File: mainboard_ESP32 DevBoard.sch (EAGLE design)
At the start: 38 parts, among them IC1 LM358N, IC2 LM833N, IC3 74HC08N, K1 AQH213, X1 JST-XH-02-PIN-LONG-PAD, X2 JST-XH-04-PIN-LONG-PAD, X3 1751248, X4 1751248

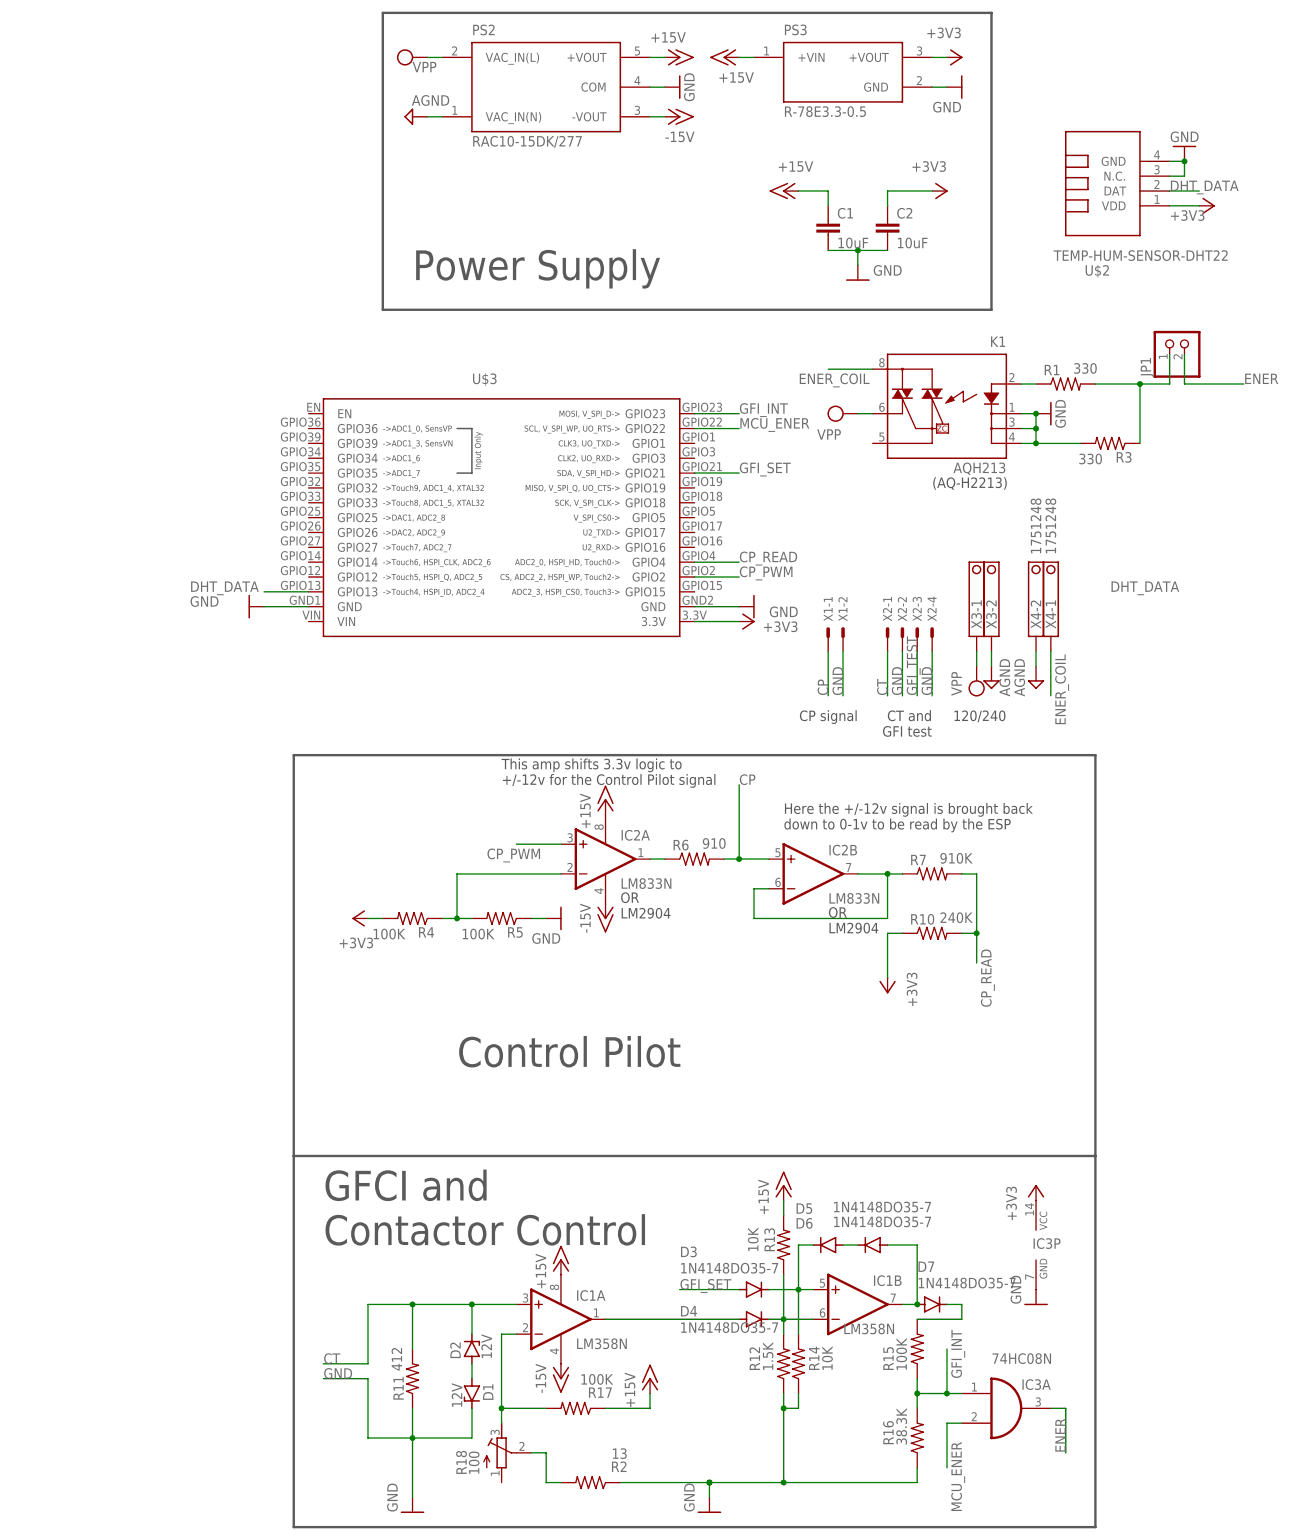
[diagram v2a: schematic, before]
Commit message: Added header to disconnect 3.3v output from esp to 3.3 rail. Added LED to indicate when contactor is energized. Added I2C connector. Added mounting holes.
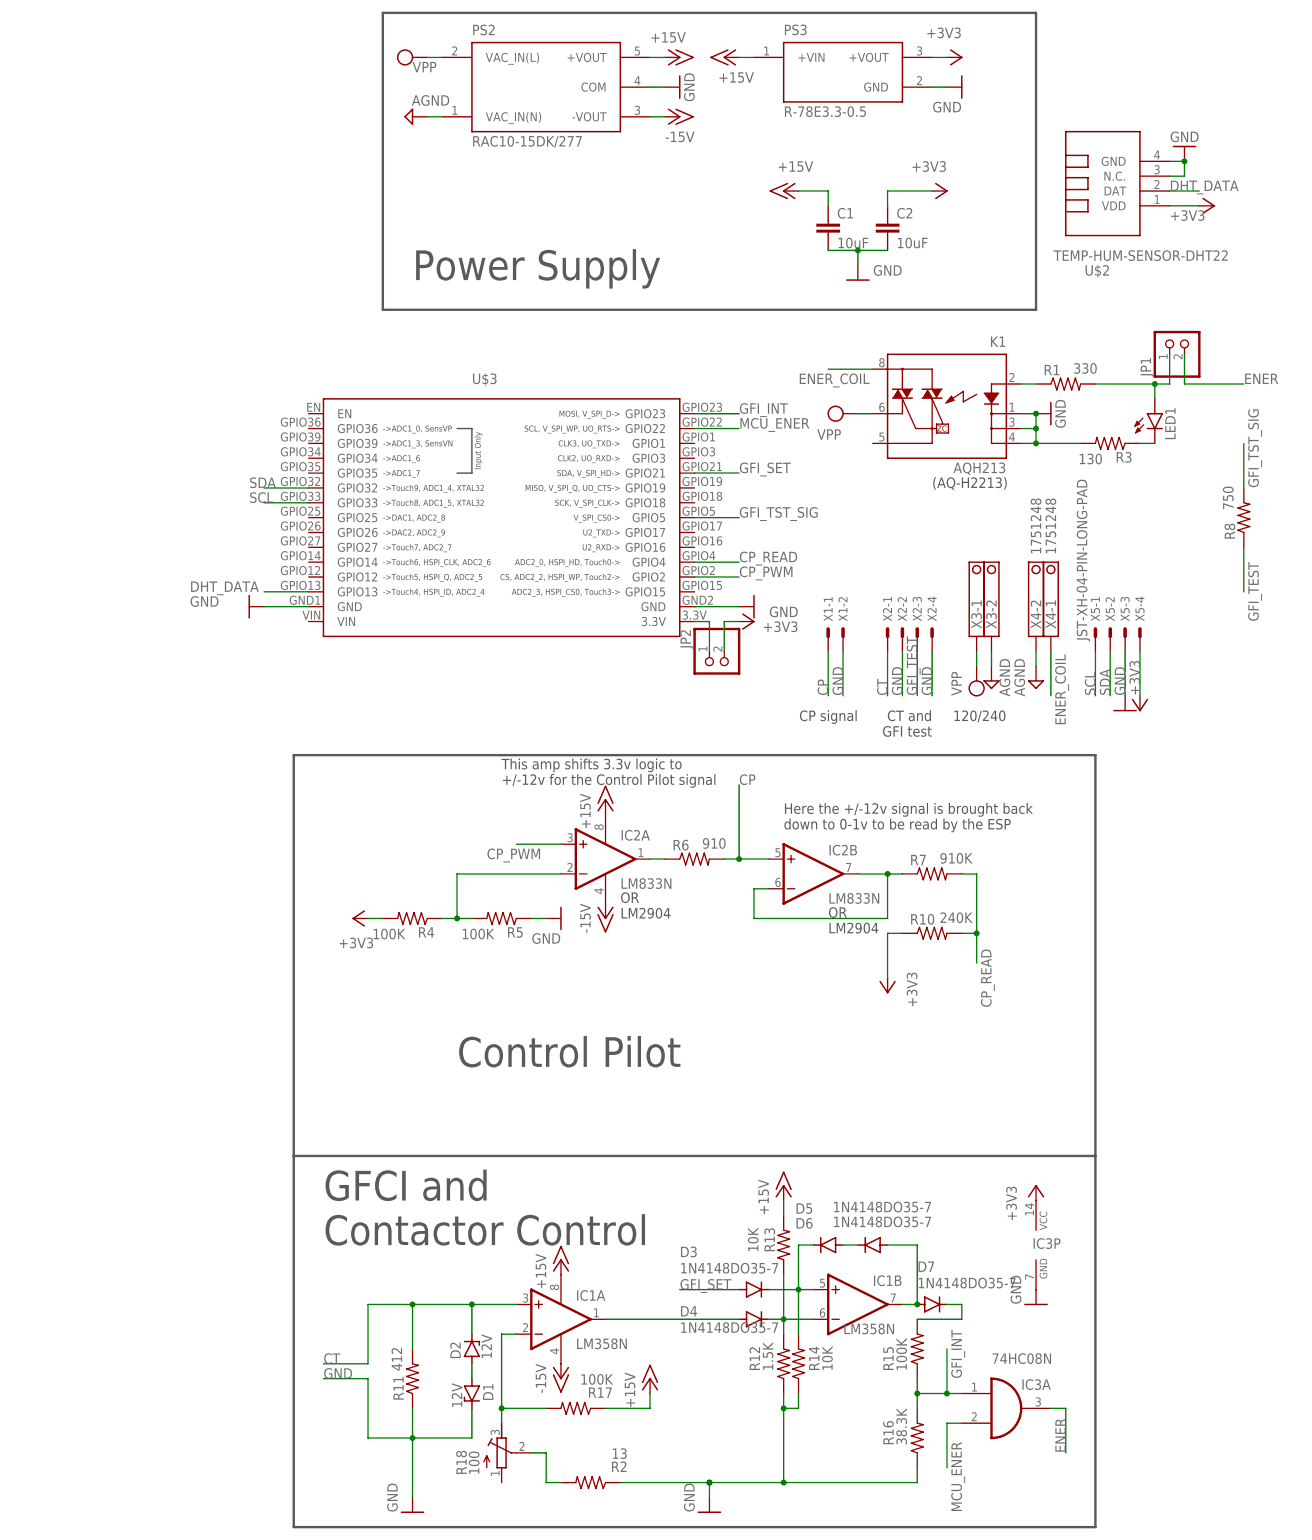
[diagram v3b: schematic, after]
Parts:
- added JP2: (no value), pinhead:PINHD-1X2/90
- added LED1: (no value), led:LED3MM
- added R8: 750, rcl:R-US_0204/7
- added X5: JST-XH-04-PIN-LONG-PAD, Rembrandt Electronics - JST XH Connectors v1-0:JST-XH-04-PIN-LONG-PAD
- R3: value 330 -> 130
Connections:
- new net GFI_TST_SIG: R8.2, U$3.GPIO5
- new net N$10: JP2.1, U$3.3.3V
- new net N$8: LED1.C, R3.1
- new net SCL: U$3.GPIO33, X5-1.S
- new net SDA: U$3.GPIO32, X5-2.S
- net +3V3: now also JP2.2, X5-4.S; no longer U$3.3.3V
- net GFI_TEST: now also R8.1
- net GND: now also X5-3.S
- net N$3: now also LED1.A; no longer R3.1
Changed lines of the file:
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@@
 <part name="GND4" library="supply1" library_urn="urn:adsk.eagle:library:371" deviceset="GND" device=""/>
 <part name="JP1" library="pinhead" library_urn="urn:adsk.eagle:library:325" deviceset="PINHD-1X2" device="" package3d_urn="urn:adsk.eagle:package:22435/2"/>
-<part name="R3" library="rcl" library_urn="urn:adsk.eagle:library:334" deviceset="R-US_" device="0204/7" package3d_urn="urn:adsk.eagle:package:23498/2" value="330"/>
+<part name="R3" library="rcl" library_urn="urn:adsk.eagle:library:334" deviceset="R-US_" device="0204/7" package3d_urn="urn:adsk.eagle:package:23498/2" value="130"/>
 <part name="P+5" library="supply1" library_urn="urn:adsk.eagle:library:371" deviceset="+15V" device=""/>
 <part name="P+6" library="supply1" library_urn="urn:adsk.eagle:library:371" deviceset="+15V" device=""/>
@@
 <part name="P+7" library="supply1" library_urn="urn:adsk.eagle:library:371" deviceset="+15V" device=""/>
 <part name="D7" library="diode" library_urn="urn:adsk.eagle:library:210" deviceset="1N4148" device="DO35-7" package3d_urn="urn:adsk.eagle:package:43339/2"/>
+<part name="LED1" library="led" library_urn="urn:adsk.eagle:library:259" deviceset="LED" device="3MM" package3d_urn="urn:adsk.eagle:package:15797/1"/>
+<part name="JP2" library="pinhead" library_urn="urn:adsk.eagle:library:325" deviceset="PINHD-1X2" device="/90" package3d_urn="urn:adsk.eagle:package:22437/2"/>
+<part name="R8" library="rcl" library_urn="urn:adsk.eagle:library:334" deviceset="R-US_" device="0204/7" package3d_urn="urn:adsk.eagle:package:23498/2" value="750"/>
+<part name="X5" library="Rembrandt Electronics - JST XH Connectors v1-0" deviceset="JST-XH-04-PIN" device="-LONG-PAD"/>
+<part name="GND7" library="supply1" library_urn="urn:adsk.eagle:library:371" deviceset="GND" device=""/>
+<part name="+3V1" library="supply1" library_urn="urn:adsk.eagle:library:371" deviceset="+3V3" device=""/>
 </parts>
 <sheets>
@@
 <text x="114.3" y="33.02" size="1.778" layer="97" rot="R180">120/240</text>
 <wire x1="7.62" y1="152.4" x2="7.62" y2="101.6" width="0.4064" layer="97"/>
-<wire x1="7.62" y1="101.6" x2="111.76" y2="101.6" width="0.4064" layer="97"/>
-<wire x1="111.76" y1="101.6" x2="111.76" y2="152.4" width="0.4064" layer="97"/>
-<wire x1="111.76" y1="152.4" x2="7.62" y2="152.4" width="0.4064" layer="97"/>
+<wire x1="7.62" y1="101.6" x2="119.38" y2="101.6" width="0.4064" layer="97"/>
+<wire x1="119.38" y1="101.6" x2="119.38" y2="152.4" width="0.4064" layer="97"/>
+<wire x1="119.38" y1="152.4" x2="7.62" y2="152.4" width="0.4064" layer="97"/>
 <text x="12.7" y="106.68" size="5.08" layer="97">Power Supply</text>
 </plain>
@@
 <attribute name="NAME" x="99.06" y="-63.0174" size="1.778" layer="95"/>
 <attribute name="VALUE" x="99.06" y="-65.8114" size="1.778" layer="96"/>
+</instance>
+<instance part="LED1" gate="G$1" x="139.7" y="83.82" smashed="yes">
+<attribute name="NAME" x="143.256" y="79.248" size="1.778" layer="95" rot="R90"/>
+<attribute name="VALUE" x="145.415" y="79.248" size="1.778" layer="96" rot="R90"/>
+</instance>
+<instance part="JP2" gate="G$1" x="66.04" y="40.64" smashed="yes" rot="MR270">
+<attribute name="NAME" x="60.325" y="46.99" size="1.778" layer="95" rot="MR270"/>
+<attribute name="VALUE" x="71.12" y="46.99" size="1.778" layer="96" rot="MR270"/>
+</instance>
+<instance part="R8" gate="G$1" x="154.94" y="66.04" smashed="yes" rot="R90">
+<attribute name="NAME" x="153.4414" y="62.23" size="1.778" layer="95" rot="R90"/>
+<attribute name="VALUE" x="153.162" y="67.31" size="1.778" layer="96" rot="R90"/>
+</instance>
+<instance part="X5" gate="-1" x="129.54" y="45.72" smashed="yes" rot="R90">
+<attribute name="NAME" x="130.302" y="48.26" size="1.524" layer="95" rot="R90"/>
+<attribute name="VALUE" x="128.143" y="44.958" size="1.778" layer="96" rot="R90"/>
+</instance>
+<instance part="X5" gate="-2" x="132.08" y="45.72" smashed="yes" rot="R90">
+<attribute name="NAME" x="132.842" y="48.26" size="1.524" layer="95" rot="R90"/>
+</instance>
+<instance part="X5" gate="-3" x="134.62" y="45.72" smashed="yes" rot="R90">
+<attribute name="NAME" x="135.382" y="48.26" size="1.524" layer="95" rot="R90"/>
+</instance>
+<instance part="X5" gate="-4" x="137.16" y="45.72" smashed="yes" rot="R90">
+<attribute name="NAME" x="137.922" y="48.26" size="1.524" layer="95" rot="R90"/>
+</instance>
+<instance part="GND7" gate="1" x="134.62" y="33.02" smashed="yes">
+<attribute name="VALUE" x="134.62" y="35.56" size="1.778" layer="96" rot="R90"/>
+</instance>
+<instance part="+3V1" gate="G$1" x="137.16" y="33.02" smashed="yes" rot="R180">
+<attribute name="VALUE" x="137.16" y="35.56" size="1.778" layer="96" rot="R90"/>
 </instance>
 </instances>
@@
 <wire x1="60.96" y1="50.8" x2="68.58" y2="50.8" width="0.1524" layer="91"/>
 </segment>
+<segment>
+<pinref part="X5" gate="-3" pin="S"/>
+<wire x1="134.62" y1="43.18" x2="134.62" y2="35.56" width="0.1524" layer="91"/>
+<pinref part="GND7" gate="1" pin="GND"/>
+</segment>
 </net>
 <net name="+3V3" class="0">
@@
 <pinref part="+3V2" gate="G$1" pin="+3V3"/>
 <wire x1="142.24" y1="119.38" x2="147.32" y2="119.38" width="0.1524" layer="91"/>
-</segment>
-<segment>
-<pinref part="+3V5" gate="G$1" pin="+3V3"/>
-<pinref part="PS3" gate="G$1" pin="+VOUT"/>
-<wire x1="104.14" y1="144.78" x2="101.6" y2="144.78" width="0.1524" layer="91"/>
 </segment>
 <segment>
@@
 <segment>
 <pinref part="+3V8" gate="G$1" pin="+3V3"/>
-<pinref part="U$3" gate="G$1" pin="3.3V"/>
-<wire x1="68.58" y1="48.26" x2="60.96" y2="48.26" width="0.1524" layer="91"/>
+<wire x1="68.58" y1="48.26" x2="66.04" y2="48.26" width="0.1524" layer="91"/>
+<pinref part="JP2" gate="G$1" pin="2"/>
+<wire x1="66.04" y1="43.18" x2="66.04" y2="48.26" width="0.1524" layer="91"/>
+</segment>
+<segment>
+<pinref part="PS3" gate="G$1" pin="+VOUT"/>
+<pinref part="+3V5" gate="G$1" pin="+3V3"/>
+<wire x1="101.6" y1="144.78" x2="104.14" y2="144.78" width="0.1524" layer="91"/>
+</segment>
+<segment>
+<pinref part="X5" gate="-4" pin="S"/>
+<wire x1="137.16" y1="43.18" x2="137.16" y2="35.56" width="0.1524" layer="91"/>
+<pinref part="+3V1" gate="G$1" pin="+3V3"/>
 </segment>
 </net>
@@
 <label x="99.06" y="35.56" size="1.778" layer="95" rot="R90"/>
 </segment>
+<segment>
+<wire x1="154.94" y1="60.96" x2="154.94" y2="53.34" width="0.1524" layer="91"/>
+<pinref part="R8" gate="G$1" pin="1"/>
+<label x="157.48" y="48.26" size="1.778" layer="95" rot="R90"/>
+</segment>
 </net>
 <net name="N$6" class="0">
@@
 <pinref part="U$3" gate="G$1" pin="GPIO13"/>
 <wire x1="-5.08" y1="53.34" x2="-12.7" y2="53.34" width="0.1524" layer="91"/>
-<label x="132.08" y="53.34" size="1.778" layer="95"/>
 <label x="-25.4" y="53.34" size="1.778" layer="95"/>
 </segment>
@@
 <pinref part="R1" gate="G$1" pin="2"/>
 <wire x1="142.24" y1="93.98" x2="142.24" y2="88.9" width="0.1524" layer="91"/>
-<wire x1="142.24" y1="88.9" x2="137.16" y2="88.9" width="0.1524" layer="91"/>
-<pinref part="R3" gate="G$1" pin="1"/>
-<wire x1="137.16" y1="88.9" x2="129.54" y2="88.9" width="0.1524" layer="91"/>
-<wire x1="137.16" y1="78.74" x2="137.16" y2="88.9" width="0.1524" layer="91"/>
-<junction x="137.16" y="88.9"/>
+<wire x1="142.24" y1="88.9" x2="139.7" y2="88.9" width="0.1524" layer="91"/>
+<pinref part="LED1" gate="G$1" pin="A"/>
+<wire x1="139.7" y1="88.9" x2="129.54" y2="88.9" width="0.1524" layer="91"/>
+<wire x1="139.7" y1="86.36" x2="139.7" y2="88.9" width="0.1524" layer="91"/>
+<junction x="139.7" y="88.9"/>
 </segment>
 </net>
@@
 </segment>
 </net>
+<net name="N$8" class="0">
+<segment>
+<pinref part="R3" gate="G$1" pin="1"/>
+<pinref part="LED1" gate="G$1" pin="C"/>
+<wire x1="139.7" y1="78.74" x2="137.16" y2="78.74" width="0.1524" layer="91"/>
+</segment>
+</net>
+<net name="N$10" class="0">
+<segment>
+<pinref part="U$3" gate="G$1" pin="3.3V"/>
+<wire x1="63.5" y1="48.26" x2="60.96" y2="48.26" width="0.1524" layer="91"/>
+<pinref part="JP2" gate="G$1" pin="1"/>
+<wire x1="63.5" y1="48.26" x2="63.5" y2="43.18" width="0.1524" layer="91"/>
+</segment>
+</net>
+<net name="GFI_TST_SIG" class="0">
+<segment>
+<pinref part="R8" gate="G$1" pin="2"/>
+<wire x1="154.94" y1="71.12" x2="154.94" y2="78.74" width="0.1524" layer="91"/>
+<label x="157.48" y="71.12" size="1.778" layer="95" rot="R90"/>
+</segment>
+<segment>
+<pinref part="U$3" gate="G$1" pin="GPIO5"/>
+<wire x1="60.96" y1="66.04" x2="68.58" y2="66.04" width="0.1524" layer="91"/>
+<label x="68.58" y="66.04" size="1.778" layer="95"/>
+</segment>
+</net>
+<net name="SDA" class="0">
+<segment>
+<pinref part="X5" gate="-2" pin="S"/>
+<wire x1="132.08" y1="43.18" x2="132.08" y2="35.56" width="0.1524" layer="91"/>
+<label x="132.08" y="35.56" size="1.778" layer="95" rot="R90"/>
+</segment>
+<segment>
+<pinref part="U$3" gate="G$1" pin="GPIO32"/>
+<wire x1="-5.08" y1="71.12" x2="-12.7" y2="71.12" width="0.1524" layer="91"/>
+<label x="-15.24" y="71.12" size="1.778" layer="95"/>
+</segment>
+</net>
+<net name="SCL" class="0">
+<segment>
+<pinref part="U$3" gate="G$1" pin="GPIO33"/>
+<wire x1="-5.08" y1="68.58" x2="-12.7" y2="68.58" width="0.1524" layer="91"/>
+<label x="-15.24" y="68.58" size="1.778" layer="95"/>
+</segment>
+<segment>
+<pinref part="X5" gate="-1" pin="S"/>
+<wire x1="129.54" y1="43.18" x2="129.54" y2="35.56" width="0.1524" layer="91"/>
+<label x="129.54" y="35.56" size="1.778" layer="95" rot="R90"/>
+</segment>
+</net>
